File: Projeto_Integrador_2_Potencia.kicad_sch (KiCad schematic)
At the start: 13 parts, among them J1 Conn_01x03_Pin, J2 Vi 24V, J3 Vo 48V, J4 Conn_01x06_Pin, Q1 IRF740, U1 INA219AxD

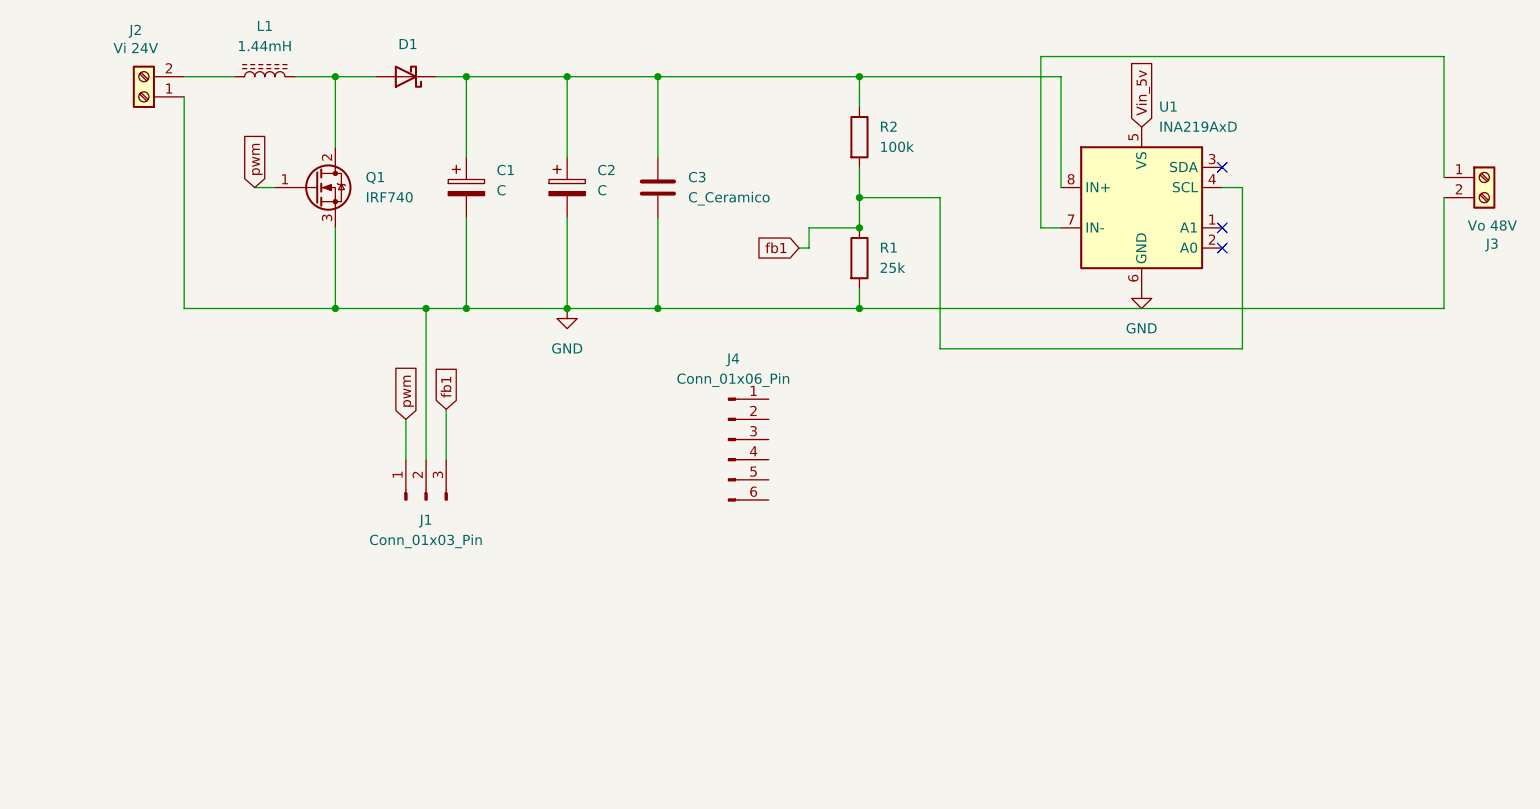
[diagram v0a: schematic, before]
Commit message: Inclusão dos soquetes para ESP32 e INA219
-Alimentação 12V para o ESP32
-Alimentação 3V3 do ESP32 para o INA
-Divisor de tensão de 48V para 5V2 para Feedback para Circuito de Comando

Falta desenvolver Layout
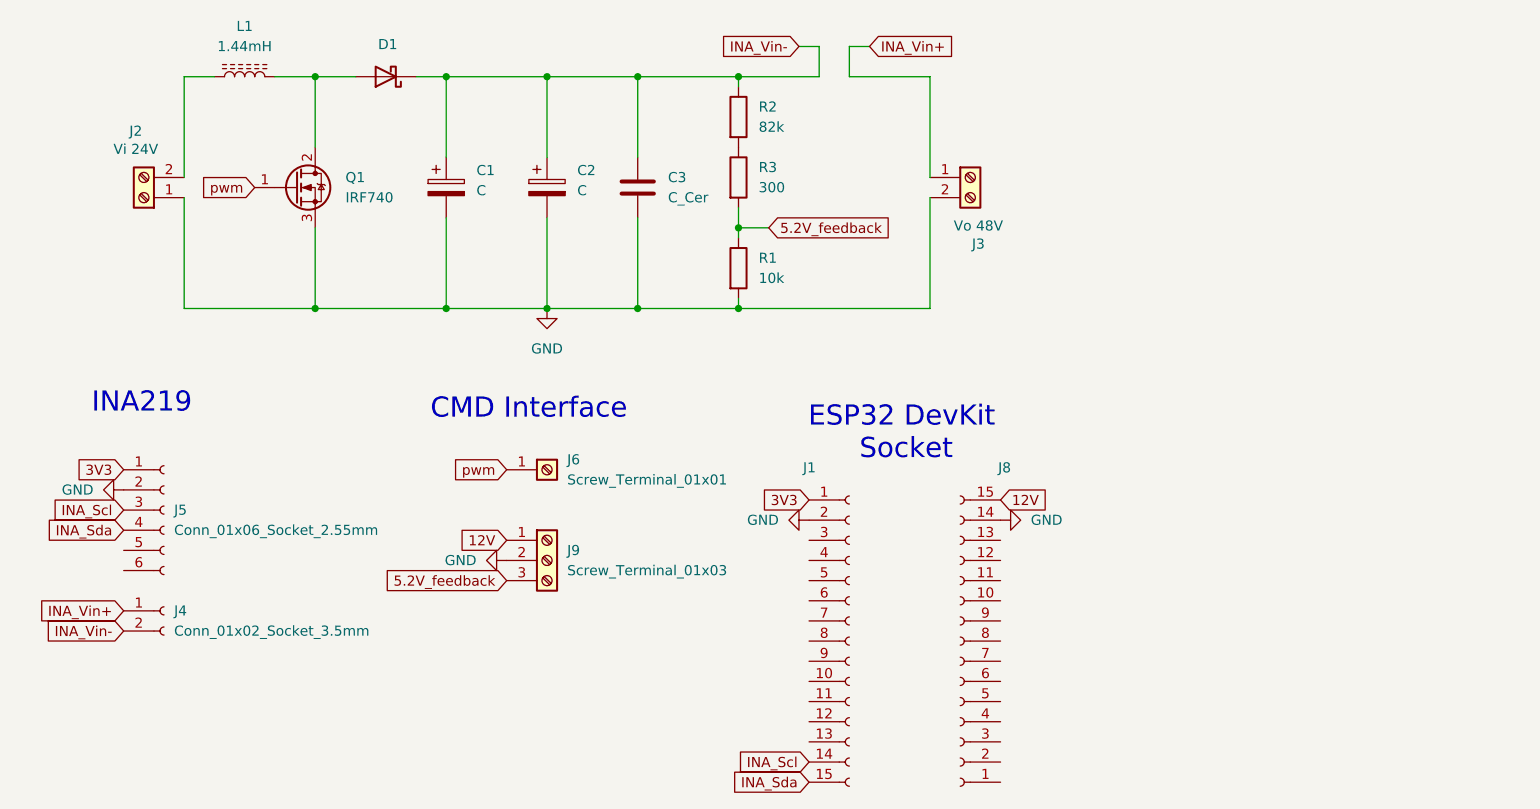
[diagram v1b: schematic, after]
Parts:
- removed J1: Conn_01x03_Pin, Connector_PinHeader_2.54mm:PinHeader_1x03_P2.54mm_Vertical, symbol Connector:Conn_01x03_Pin
- removed J4: Conn_01x06_Pin, symbol Connector:Conn_01x06_Pin
- removed U1: INA219AxD, Package_SO:SOIC-8_3.9x4.9mm_P1.27mm, symbol Sensor_Energy:INA219AxD
- added J1, J8: ~, symbol Connector:Conn_01x15_Socket
- added J4: Conn_01x02_Socket_3.5mm, symbol Connector:Conn_01x02_Socket
- added J5: Conn_01x06_Socket_2.55mm, symbol Connector:Conn_01x06_Socket
- added J6: Screw_Terminal_01x01, symbol Connector:Screw_Terminal_01x01
- added J9: Screw_Terminal_01x03, symbol Connector:Screw_Terminal_01x03
- added R3: 300, symbol Device:R
- C3: value C_Ceramico -> C_Cer
- R1: value 25k -> 10k
- R2: value 100k -> 82k
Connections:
- net GND: now also J1.2 (Pin_2), J5.2 (Pin_2), J8.14 (Pin_14), J9.2 (Pin_2)
- net pwm: now also J6.1 (Pin_1)
- net INA_Vin-: now reaches C1.1, C2.1, C3.1, D1.1 (K), R2.1
- net INA_Vin-: now also J4.2 (Pin_2)
- net INA_Vin+: now reaches J3.1 (Pin_1)
- net INA_Vin+: now also J4.1 (Pin_1)
- net fb1: no longer names the net of R2.2
- net fb1: now also R3.1; no longer R1.1
- new net 12V: J8.15 (Pin_15), J9.1 (Pin_1)
- new net 3V3: J1.1 (Pin_1), J5.1 (Pin_1)
- new net 5.2V_feedback: J9.3 (Pin_3), R1.1, R3.2
- new net INA_Scl: J1.14 (Pin_14), J5.3 (Pin_3)
- new net INA_Sda: J1.15 (Pin_15), J5.4 (Pin_4)
- no-connect marks 3 -> 0
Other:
- note added: "CMD Interface"
- note added: "ESP32 DevKit Socket"
- note added: "INA219"
- moved on the sheet: C1, C2, C3, D1, J2, J3, L1, Q1, R1, R2
